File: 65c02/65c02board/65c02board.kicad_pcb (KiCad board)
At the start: 2 copper layers, 6 parts, among them J1 Conn_01x34_Male, U1 W65C02, U2 74HC00

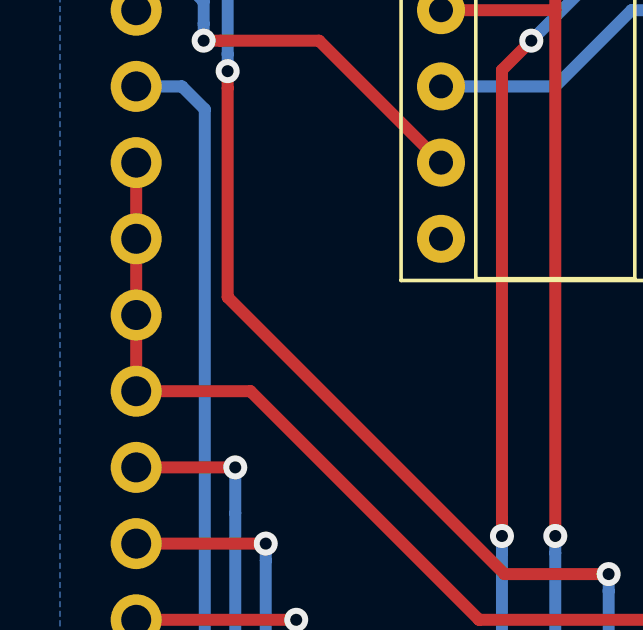
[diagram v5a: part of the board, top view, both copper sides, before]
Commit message: Modify memory map for the 65c02 to allow the P8088 to use the common rom image for simple test program without clashing.
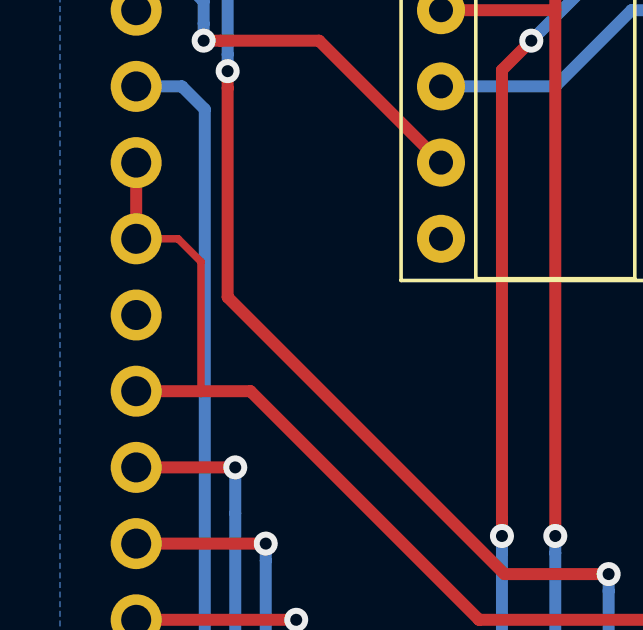
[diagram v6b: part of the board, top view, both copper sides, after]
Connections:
- J1 pad 10: /5V -> /GND
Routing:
- net /5V: track 172.2 -> 173.9 mm
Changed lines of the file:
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@@
     (thickness 1.6)
     (drawings 0)
-    (tracks 203)
+    (tracks 205)
     (zones 0)
     (modules 6)
@@
   )
   (setup
-    (last_trace_width 0.4)
+    (last_trace_width 0.25)
     (user_trace_width 0.4)
     (user_trace_width 1)
@@
       (net 1 /5V))
     (pad 10 thru_hole oval (at 0 -22.86 180) (size 1.7 1.7) (drill 1) (layers *.Cu *.Mask)
-      (net 1 /5V))
+      (net 33 /GND))
     (pad 11 thru_hole oval (at 0 -25.4 180) (size 1.7 1.7) (drill 1) (layers *.Cu *.Mask)
       (net 1 /5V))
@@
   (segment (start 137.16 124.46) (end 137.16 128.27) (width 0.4) (layer F.Cu) (net 1))
   (segment (start 137.16 128.27) (end 135.89 129.54) (width 0.4) (layer F.Cu) (net 1))
-  (segment (start 127 76.2) (end 127 73.66) (width 0.4) (layer F.Cu) (net 1))
-  (segment (start 127 73.66) (end 127 71.12) (width 0.4) (layer F.Cu) (net 1))
   (segment (start 127 71.12) (end 127 68.58) (width 0.4) (layer F.Cu) (net 1))
   (segment (start 145.91137 68.58) (end 149.86 68.58) (width 0.4) (layer F.Cu) (net 1))
@@
   (segment (start 149.86 68.58) (end 149.86 81.28) (width 1) (layer F.Cu) (net 1))
   (segment (start 144.78 68.58) (end 144.78 66.04) (width 0.4) (layer F.Cu) (net 1))
-  (segment (start 130.81 76.2) (end 127 76.2) (width 0.4) (layer F.Cu) (net 1))
   (segment (start 147.36 83.82) (end 138.43 83.82) (width 0.4) (layer F.Cu) (net 1))
   (segment (start 138.43 83.82) (end 130.81 76.2) (width 0.4) (layer F.Cu) (net 1))
   (segment (start 147.36 81.32) (end 147.32 81.28) (width 0.4) (layer F.Cu) (net 1))
   (segment (start 147.36 83.82) (end 147.36 81.32) (width 0.4) (layer F.Cu) (net 1))
+  (segment (start 129.159 76.2) (end 129.159 71.882) (width 0.25) (layer F.Cu) (net 1))
+  (segment (start 129.159 76.2) (end 127 76.2) (width 0.4) (layer F.Cu) (net 1))
+  (segment (start 130.81 76.2) (end 129.159 76.2) (width 0.4) (layer F.Cu) (net 1))
+  (segment (start 128.397 71.12) (end 127 71.12) (width 0.25) (layer F.Cu) (net 1))
+  (segment (start 129.159 71.882) (end 128.397 71.12) (width 0.25) (layer F.Cu) (net 1))
+  (segment (start 134.366 58.42) (end 137.16 58.42) (width 0.4) (layer F.Cu) (net 2))
+  (segment (start 127 55.88) (end 131.826 55.88) (width 0.4) (layer F.Cu) (net 2))
+  (segment (start 131.826 55.88) (end 134.366 58.42) (width 0.4) (layer F.Cu) (net 2))
+  (segment (start 137.16 63.5) (end 140.97 63.5) (width 0.4) (layer F.Cu) (net 2))
+  (segment (start 140.97 59.944) (end 140.97 63.5) (width 0.4) (layer F.Cu) (net 2))
+  (segment (start 137.16 58.42) (end 139.446 58.42) (width 0.4) (layer F.Cu) (net 2))
+  (segment (start 139.446 58.42) (end 140.97 59.944) (width 0.4) (layer F.Cu) (net 2))
+  (via (at 140.97 81.026) (size 0.8) (drill 0.4) (layers F.Cu B.Cu) (net 2))
+  (segment (start 140.97 63.5) (end 140.97 81.026) (width 0.4) (layer F.Cu) (net 2))
+  (segment (start 134.62 127) (end 140.97 120.65) (width 0.4) (layer B.Cu) (net 2))
+  (segment (start 140.97 120.65) (end 140.97 81.591685) (width 0.4) (layer B.Cu) (net 2))
+  (segment (start 140.97 81.591685) (end 140.97 81.026) (width 0.4) (layer B.Cu) (net 2))
   (segment (start 133.604 93.98) (end 130.302 90.678) (width 0.4) (layer B.Cu) (net 3))
   (segment (start 134.62 93.98) (end 133.604 93.98) (width 0.4) (layer B.Cu) (net 3))
   (segment (start 130.302 90.678) (end 130.302 80.264) (width 0.4) (layer B.Cu) (net 3))
+  (via (at 130.302 78.74) (size 0.8) (drill 0.4) (layers F.Cu B.Cu) (net 3))
+  (segment (start 130.302 80.264) (end 130.302 78.74) (width 0.4) (layer B.Cu) (net 3))
+  (segment (start 130.302 78.74) (end 127 78.74) (width 0.4) (layer F.Cu) (net 3))
   (segment (start 127 81.28) (end 131.317998 81.28) (width 0.4) (layer F.Cu) (net 4))
   (segment (start 131.317998 81.28) (end 131.318 81.279998) (width 0.4) (layer F.Cu) (net 4))
@@
   (segment (start 132.08 129.54) (end 132.08 119.38) (width 0.4) (layer F.Cu) (net 25))
   (segment (start 144.78 60.96) (end 144.78 58.42) (width 0.4) (layer F.Cu) (net 30))
-  (segment (start 134.366 58.42) (end 137.16 58.42) (width 0.4) (layer F.Cu) (net 2))
-  (segment (start 127 55.88) (end 131.826 55.88) (width 0.4) (layer F.Cu) (net 2))
-  (segment (start 131.826 55.88) (end 134.366 58.42) (width 0.4) (layer F.Cu) (net 2))
-  (segment (start 137.16 63.5) (end 140.97 63.5) (width 0.4) (layer F.Cu) (net 2))
-  (segment (start 140.97 59.944) (end 140.97 63.5) (width 0.4) (layer F.Cu) (net 2))
-  (segment (start 137.16 58.42) (end 139.446 58.42) (width 0.4) (layer F.Cu) (net 2))
-  (segment (start 139.446 58.42) (end 140.97 59.944) (width 0.4) (layer F.Cu) (net 2))
-  (via (at 140.97 81.026) (size 0.8) (drill 0.4) (layers F.Cu B.Cu) (net 2))
-  (segment (start 140.97 63.5) (end 140.97 81.026) (width 0.4) (layer F.Cu) (net 2))
-  (segment (start 134.62 127) (end 140.97 120.65) (width 0.4) (layer B.Cu) (net 2))
-  (segment (start 140.97 120.65) (end 140.97 81.591685) (width 0.4) (layer B.Cu) (net 2))
-  (segment (start 140.97 81.591685) (end 140.97 81.026) (width 0.4) (layer B.Cu) (net 2))
-  (via (at 130.302 78.74) (size 0.8) (drill 0.4) (layers F.Cu B.Cu) (net 3))
-  (segment (start 130.302 80.264) (end 130.302 78.74) (width 0.4) (layer B.Cu) (net 3))
-  (segment (start 130.302 78.74) (end 127 78.74) (width 0.4) (layer F.Cu) (net 3))
   (segment (start 137.16 55.88) (end 139.954 55.88) (width 0.4) (layer F.Cu) (net 30))
   (segment (start 142.494 58.42) (end 144.78 58.42) (width 0.4) (layer F.Cu) (net 30))
